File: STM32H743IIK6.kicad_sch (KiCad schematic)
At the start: 51 parts, among them J6 BAT, SW1 SW_Push, SW2 SW_Push, SW3 SW_Push, SW4 SW_Push, U2 STM32H743IITx, U8 TLV75733PDBV, Y1 25MHz, Y2 32.768KHz

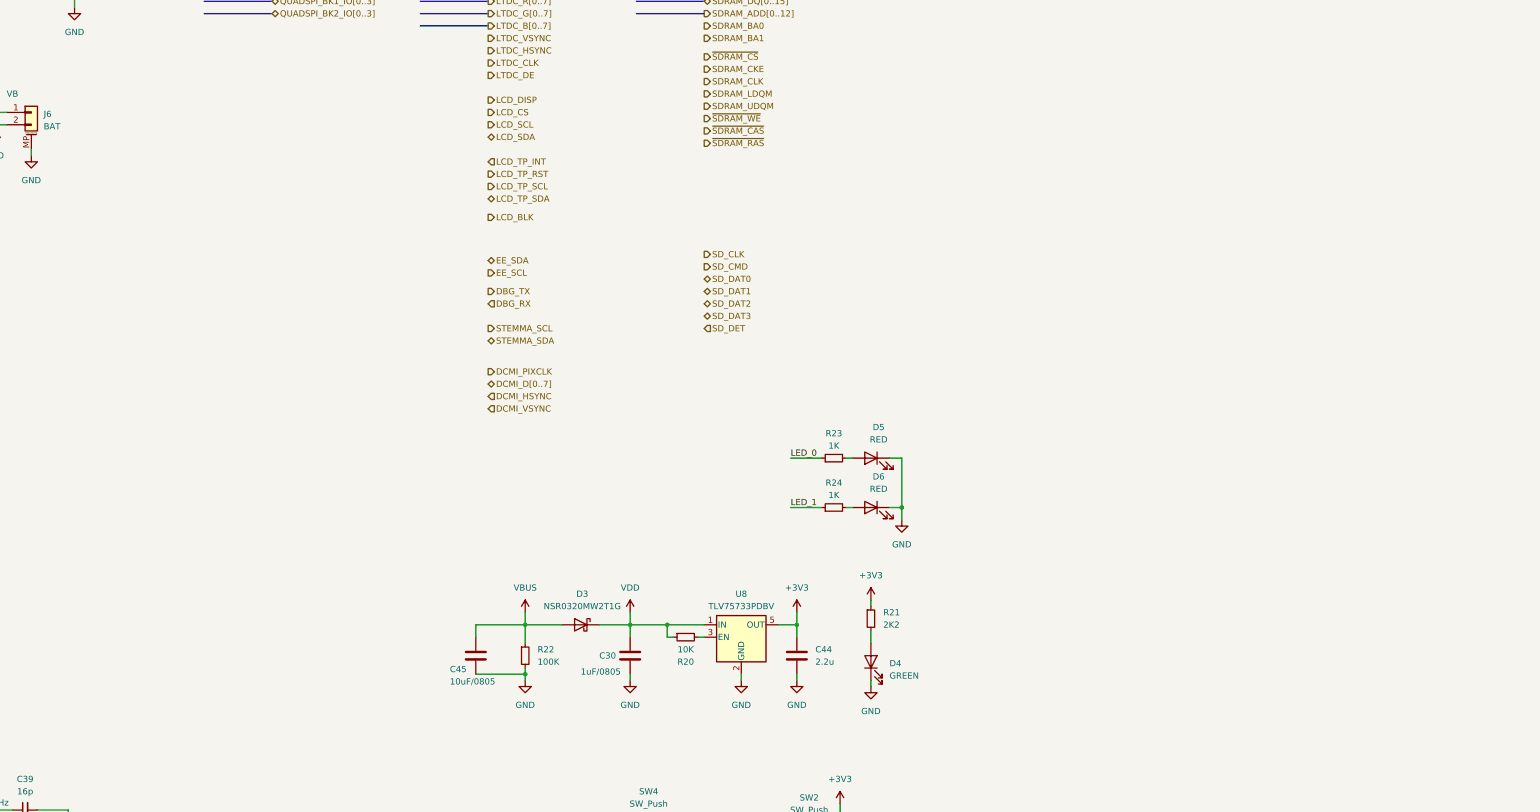
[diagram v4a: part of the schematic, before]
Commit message: Finished SDRAM, QSPI Flash, Planning to move to 5 inch orient display dimension
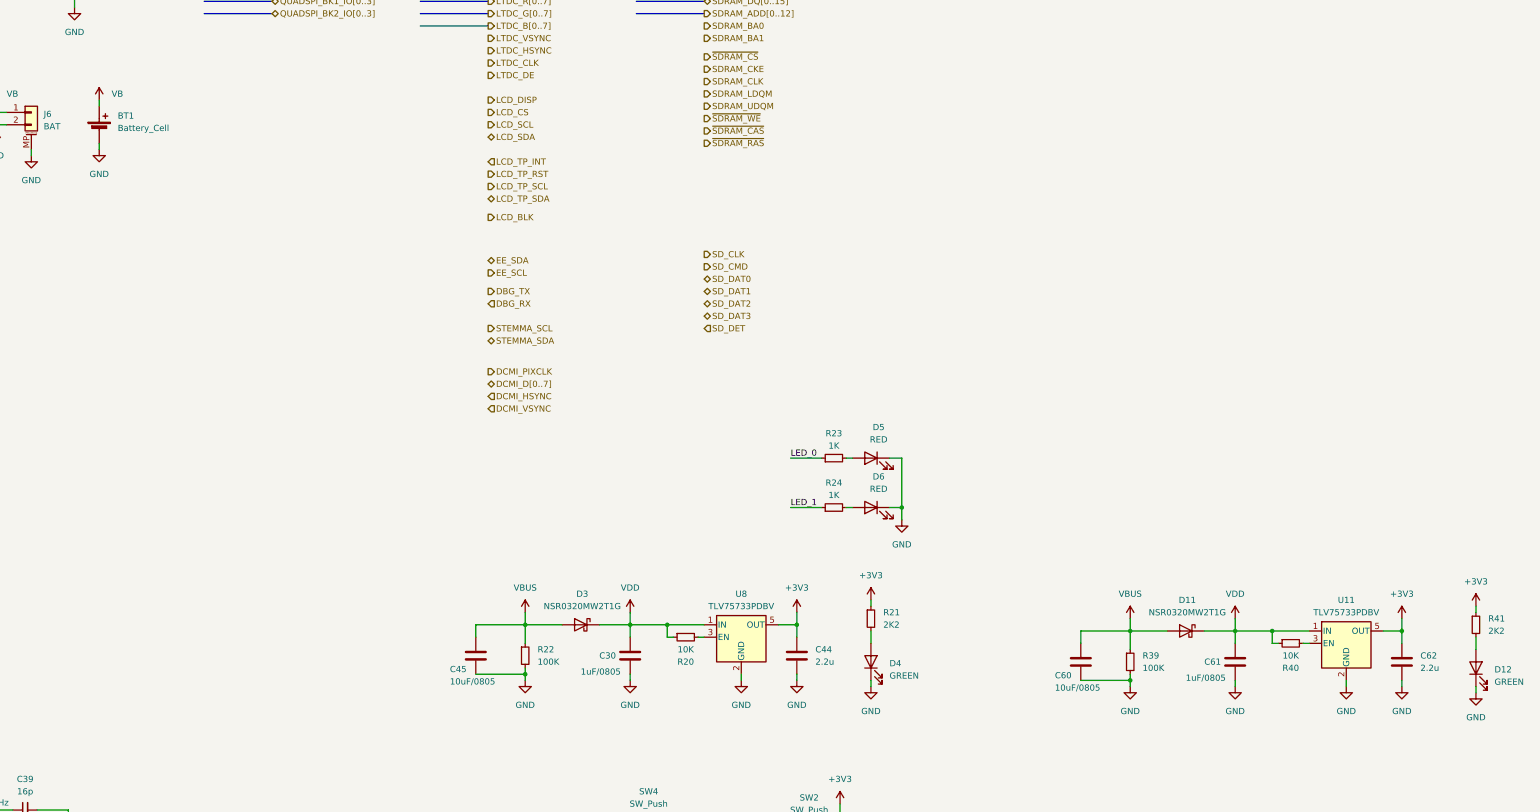
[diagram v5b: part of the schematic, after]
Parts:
- added BT1: Battery_Cell, Battery:BatteryHolder_Keystone_2998_1x6.8mm, symbol Device:Battery_Cell
- added C60: 10uF/0805, Capacitor_SMD:C_0805_2012Metric, symbol Device:C
- added C61: 1uF/0805, Capacitor_SMD:C_0805_2012Metric, symbol Device:C
- added C62: 2.2u, Capacitor_SMD:C_0805_2012Metric, symbol Device:C
- added D11: NSR0320MW2T1G, Diode_SMD:D_SOD-323, symbol Diode:NSR0340HT1G
- added D12: GREEN, LED_SMD:LED_0805_2012Metric, symbol Device:LED
- added R39: 100K, Resistor_SMD:R_0402_1005Metric, symbol Device:R_Small
- added R40: 10K, Resistor_SMD:R_0402_1005Metric, symbol Device:R_Small
- added R41: 2K2, Resistor_SMD:R_0402_1005Metric, symbol Device:R_Small
- added U11: TLV75733PDBV, Package_TO_SOT_SMD:SOT-23-5, symbol Regulator_Linear:TLV75733PDBV
- U2: JLCPCB Part # (none) -> C89597
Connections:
- net +3V3: now also C62.1, R41.1, U11.5 (OUT)
- net GND: now also BT1.2 (-), C60.2, C61.2, C62.2, D12.1 (K), R39.2, U11.2 (GND)
- net VB: now also BT1.1 (+)
- net VBUS: now also C60.1, D11.2 (A), R39.1
- net VDD: now also C61.1, D11.1 (K), R40.1, U11.1 (IN)
- new net: R40.2, U11.3 (EN)
- new net: D12.2 (A), R41.2

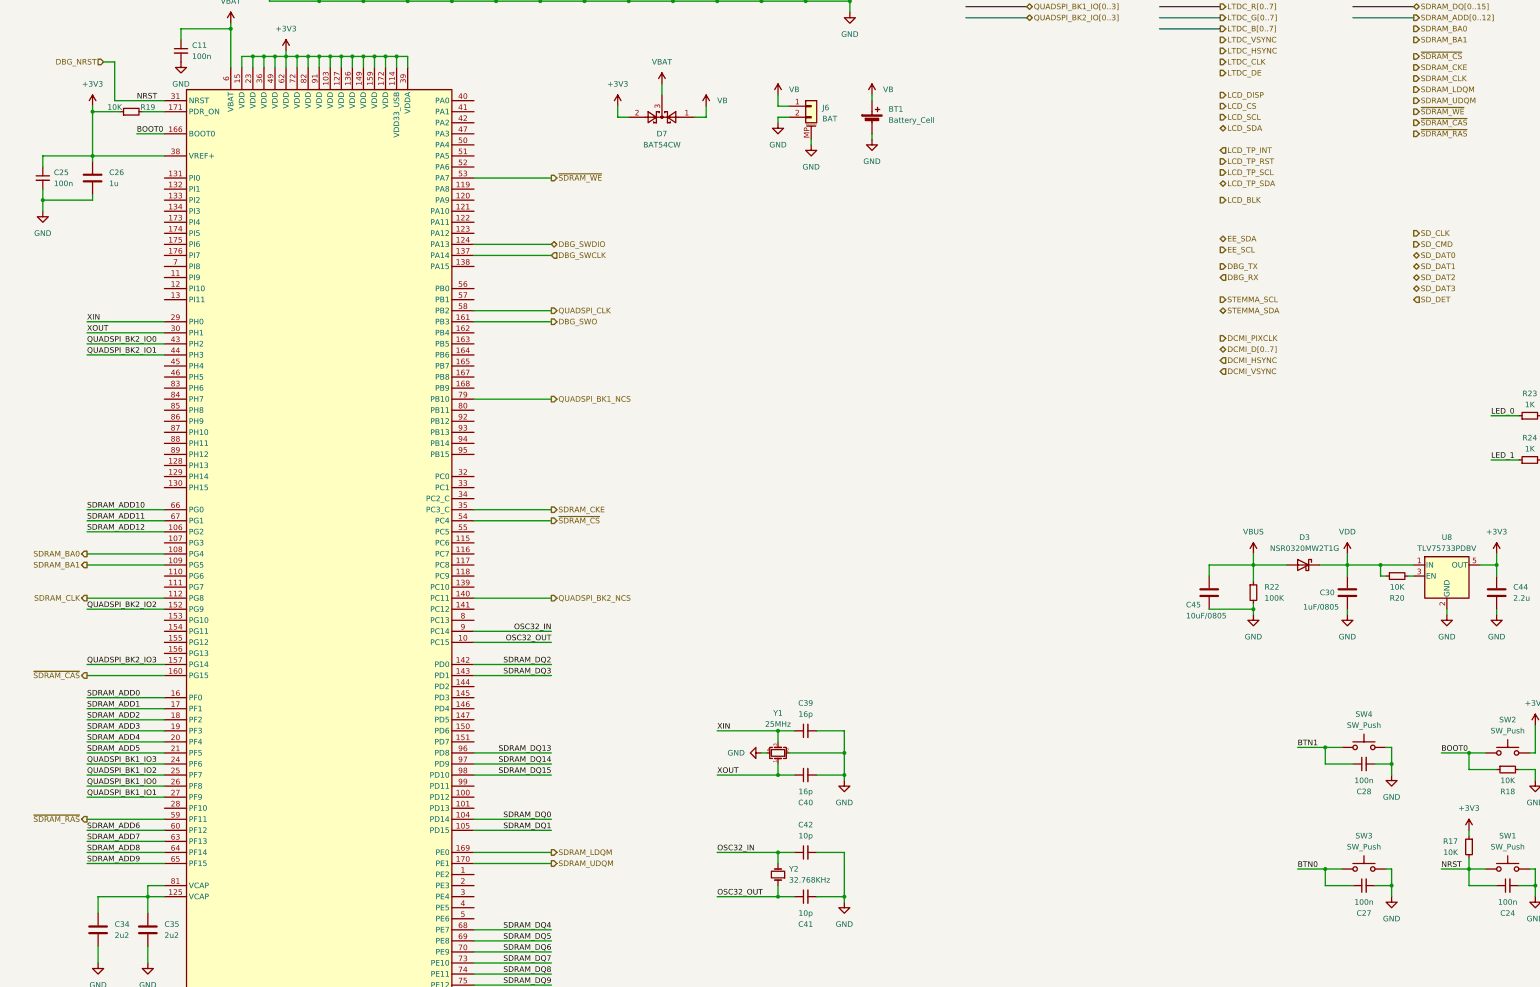
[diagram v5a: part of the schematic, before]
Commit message: Changes: USB C to midmount, CR1220 socket, flip MCU to shorten the LCD traces
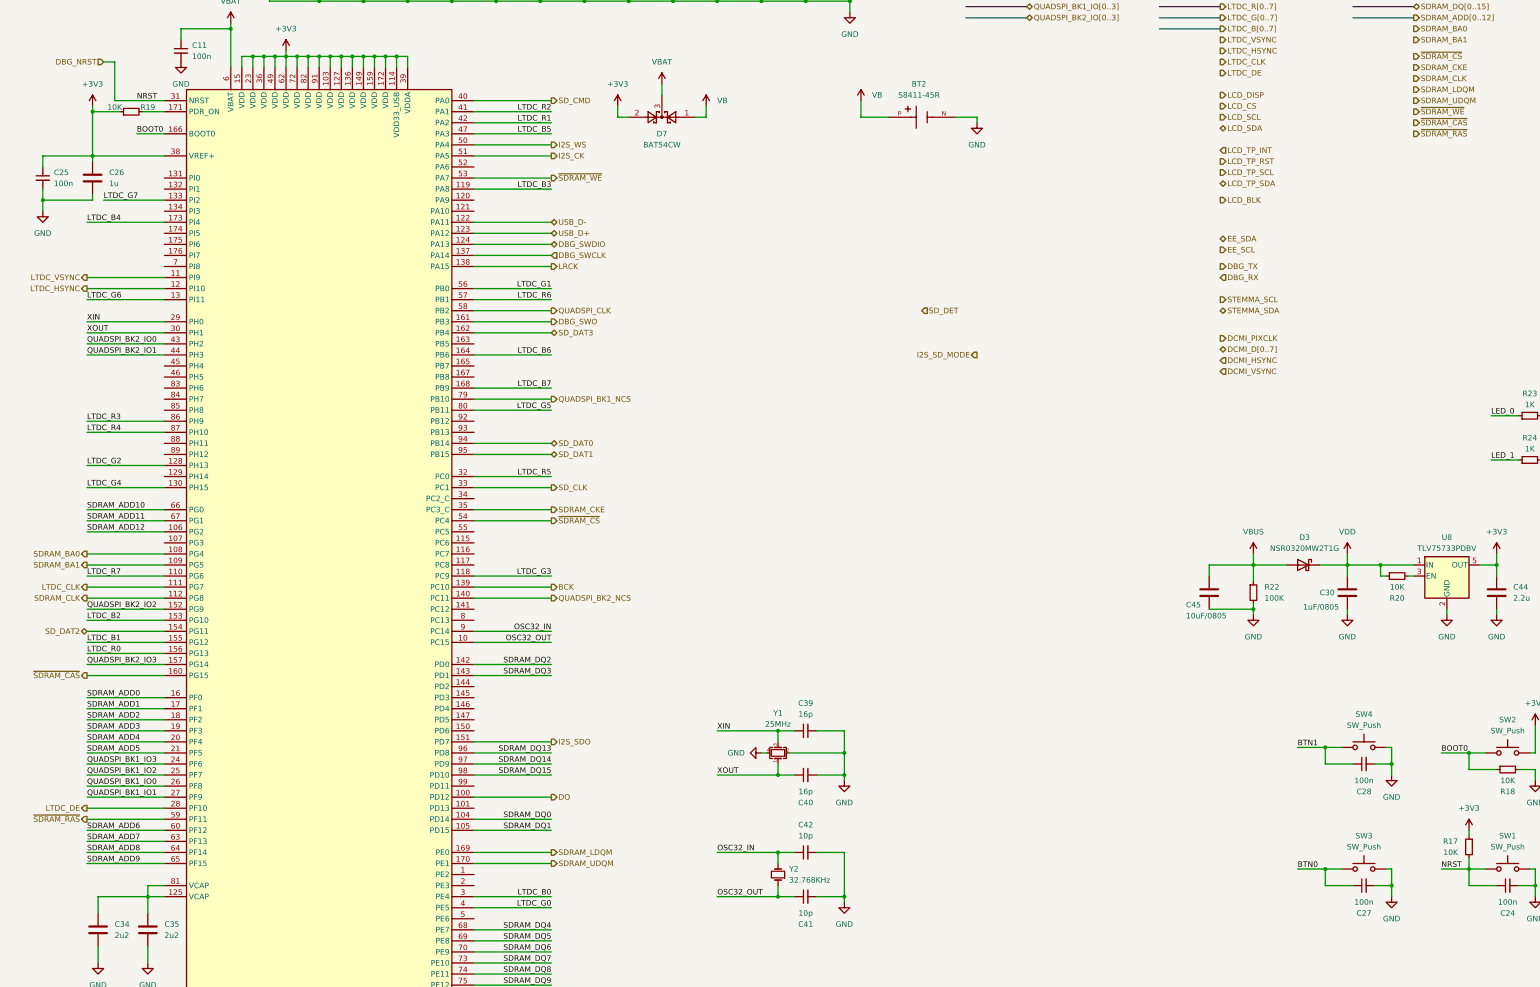
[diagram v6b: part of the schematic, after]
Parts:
- removed BT1: Battery_Cell, Battery:BatteryHolder_Keystone_2998_1x6.8mm, symbol Device:Battery_Cell
- removed J6: BAT, Connector_Hirose:Hirose_DF13C_CL535-0402-2-51_1x02-1MP_P1.25mm_Vertical, symbol Connector_Generic_MountingPin:Conn_01x02_MountingPin
- added BT2: S8411-45R, CR1220-Batt-conn-S8411-45R:CR1220-Batt-conn-S8411-45R, symbol CR1220-Batt-conn-S8411-45R:S8411-45R
- D7: footprint Package_TO_SOT_SMD:SOT-323_SC-70 -> Package_TO_SOT_SMD:SOT-23
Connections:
- net GND: now also BT2.N
- net LTDC_CLK: now also U2.111 (PG7)
- net LTDC_DE: now also U2.28 (PF10)
- net LTDC_HSYNC: now also U2.12 (PI10)
- net LTDC_VSYNC: now also U2.11 (PI9)
- net SD_CLK: now also U2.33 (PC1)
- net SD_CMD: now also U2.40 (PA0)
- net SD_DAT0: now also U2.94 (PB14)
- net SD_DAT1: now also U2.95 (PB15)
- net SD_DAT2: now also U2.154 (PG11)
- net SD_DAT3: now also U2.162 (PB4)
- net VB: now also BT2.P
- net DO: now reaches U2.100 (PD12)
- net LTDC_R7: now reaches U2.110 (PG6)
- net LTDC_G3: now reaches U2.118 (PC9)
- net LTDC_B3: now reaches U2.119 (PA8)
- net USB_D-: now reaches U2.122 (PA11)
- net USB_D+: now reaches U2.123 (PA12)
- net LTDC_G2: now reaches U2.128 (PH13)
- net LTDC_G6: now reaches U2.13 (PI11)
- net LTDC_G4: now reaches U2.130 (PH15)
- net LTDC_G7: now reaches U2.133 (PI2)
- net LRCK: now reaches U2.138 (PA15)
- net BCK: now reaches U2.139 (PC10)
- net I2S_SDO: now reaches U2.151 (PD7)
- net LTDC_B2: now reaches U2.153 (PG10)
- net LTDC_B1: now reaches U2.155 (PG12)
- net LTDC_R0: now reaches U2.156 (PG13)
- net LTDC_B6: now reaches U2.164 (PB6)
- net LTDC_B7: now reaches U2.168 (PB9)
- net LTDC_B4: now reaches U2.173 (PI4)
- net LTDC_B0: now reaches U2.3 (PE4)
- net LTDC_R5: now reaches U2.32 (PC0)
- net LTDC_G0: now reaches U2.4 (PE5)
- net LTDC_R2: now reaches U2.41 (PA1)
- net LTDC_R1: now reaches U2.42 (PA2)
- net LTDC_B5: now reaches U2.47 (PA3)
- net I2S_WS: now reaches U2.50 (PA4)
- net I2S_CK: now reaches U2.51 (PA5)
- net LTDC_G1: now reaches U2.56 (PB0)
- net LTDC_R6: now reaches U2.57 (PB1)
- net LTDC_G5: now reaches U2.80 (PB11)
- net LTDC_R3: now reaches U2.86 (PH9)
- net LTDC_R4: now reaches U2.87 (PH10)

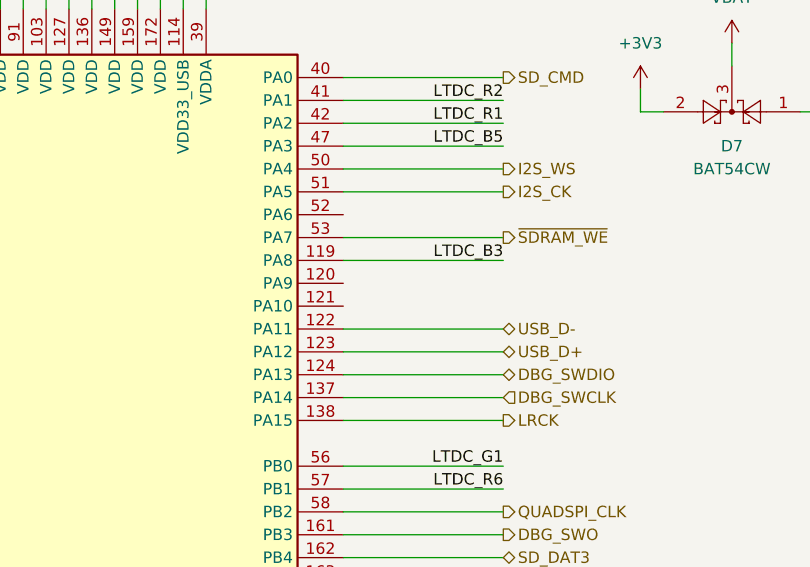
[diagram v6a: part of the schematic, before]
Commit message: Finished SDRAM, LTDC, QSPI, SDMMC, still an error on LTDC B channel
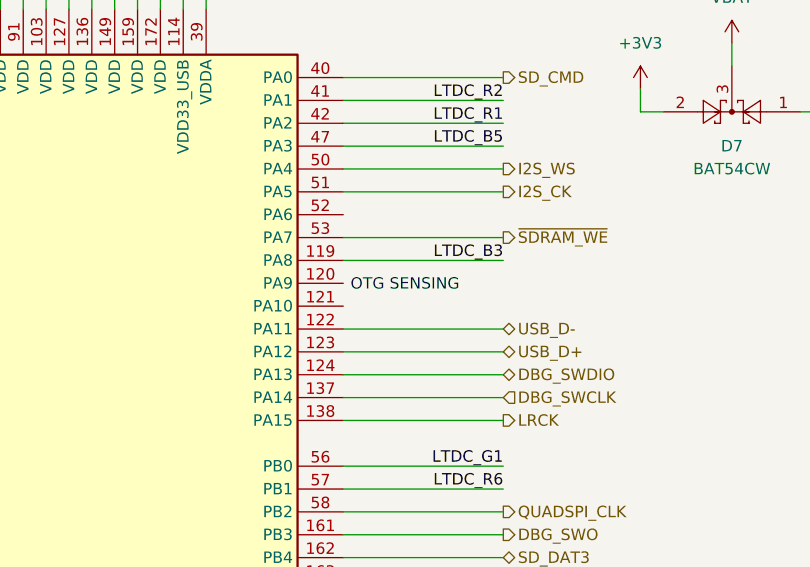
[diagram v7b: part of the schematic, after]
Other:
- note added: "OTG SENSING"
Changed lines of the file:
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@@
+		)
+	)
+	(text "OTG SENSING"
+		(exclude_from_sim no)
+		(at 136.398 78.994 0)
+		(effects
+			(font
+				(size 1.27 1.27)
+			)
 		)
 	)

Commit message: Finished SDRAM, QSPI, SDMMC, LTDC, TP, EEPROM, USB, debug (need to verify on UART)
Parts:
- added Q2, Q3: MMBT3904, Package_TO_SOT_SMD:SOT-23, symbol Transistor_BJT:MMBT3904
- added R49, R51: 47K, Resistor_SMD:R_0402_1005Metric, symbol Device:R_Small
- added R50, R52: 10K, Resistor_SMD:R_0402_1005Metric, symbol Device:R_Small
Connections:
- net +3V3: now also R23.2, R24.2
- net EE_SCL: now also U2.45 (PH4)
- net EE_SDA: now also U2.46 (PH5)
- net GND: now also Q2.2 (E), Q3.2 (E), R50.2, R52.2; no longer D5.1 (K), D6.1 (K)
- net LCD_BLK: now also U2.163 (PB5)
- net LCD_TP_INT: now also U2.144 (PD2)
- net LCD_TP_RST: now also U2.146 (PD4)
- net LCD_TP_SCL: now also U2.164 (PB6)
- net LCD_TP_SDA: now also U2.165 (PB7)
- net LED_0: now also R49.1; no longer R23.1
- net LED_1: now also R51.1; no longer R24.1
- net LTDC_B6: now also U2.167 (PB8); no longer U2.164 (PB6)
- net at D6.2 (A): now also R24.1; no longer R24.2
- net at D5.2 (A): now also R23.1; no longer R23.2
- new net: Q2.1 (B), R49.2, R50.1
- new net: Q3.1 (B), R51.2, R52.1
- new net: D5.1 (K), Q2.3 (C)
- new net: D6.1 (K), Q3.3 (C)
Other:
- moved on the sheet: D5, D6, R23, R24
